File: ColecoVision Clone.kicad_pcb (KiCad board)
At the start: 2 copper layers, 149.4 x 99.1 mm, 143 parts, among them J1 Cartridge Slot, J2 Composite video, J3 PJ-102A, J4 RCJ-017, J5 Controller Port 1, J6 Controller Port 2, Q1 2n4401, Q2 Q_NJFET_DGS, Q3 2N3904, Q4 2N3904, Q5 2N3904, SW1 Power Toggle, SW2 Reset, U1 Z80CPU, U10 SN76489AN, U12 74LS138 (Mem. Mapped), U13 74LS138 (I/O), U14 74LS02, U15 Controller 1, U16 Controller 2, U17 74LS05, U18 74LS05, U19 74HC04, U2 Work RAM, U20 74LS74, U21 74HC04, U22 74LS74, U23 74HCT00, U24 TPS60403DBVR, U3 BIOS ROM 27C256, U4 74HCT04, U5 TMS9918A, U6 74LS574, U7 74LS574, U8 74LS574, U9 VRAM, X1 14.31818MHz

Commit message: powering chips
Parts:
- C4, R15: moved to B.Cu
- moved R1 191.3 mm to (24.6, 47.9)
- moved C4 99.2 mm to (52.5, 39.9), turned to 90 degrees
- moved R15 90.1 mm to (32.3, 67.6), turned to 90 degrees
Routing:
- net VCC: track 650.9 -> 742.4 mm, vias 30 -> 39
- net GND: track 745.0 -> 771.3 mm, vias 38 -> 40
- net !WAIT: track 125.4 -> 134.8 mm
- net /Video/VIDVCC: track 4.64 -> 11.0 mm
- net AD1: track 105.0 -> 98.9 mm
- net Net-(R15-Pad2): track 0.00 -> 4.93 mm
- net RW: track 71.8 -> 75.1 mm
- net D1: track 289.9 -> 288.8 mm
- net RAM_A1: track 23.7 -> 22.7 mm
- net RAM_A0: track 24.1 -> 23.4 mm
- net AD3: track 91.3 -> 92.0 mm
- net AD0: track 96.5 -> 95.9 mm

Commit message: HALT pullup
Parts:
- removed TP13: TestPoint, Measurement_Points:Measurement_Point_Round-SMD-Pad_Small
- R44: moved to B.Cu
- moved R44 307.0 mm to (-56.0, 82.7)
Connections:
- net !HALT renamed Net-(R44-Pad2)
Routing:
- net Net-(R44-Pad2): track 5.94 -> 44.9 mm, vias 1 -> 8
- net VCC: track 742.4 -> 749.3 mm, vias 39 -> 40
- net D3: track 270.1 -> 269.6 mm

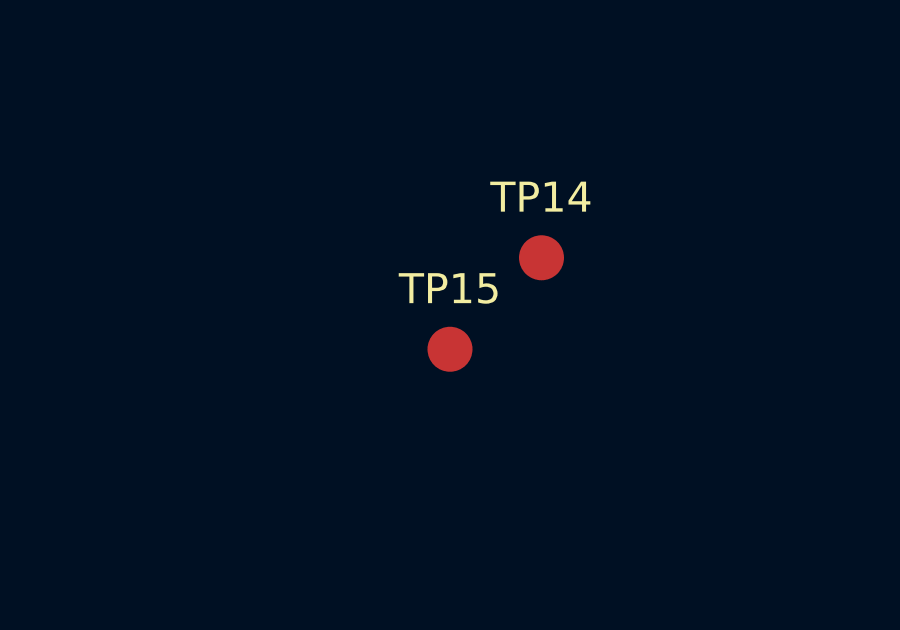
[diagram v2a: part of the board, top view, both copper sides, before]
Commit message: Goodbye A15 testpoint
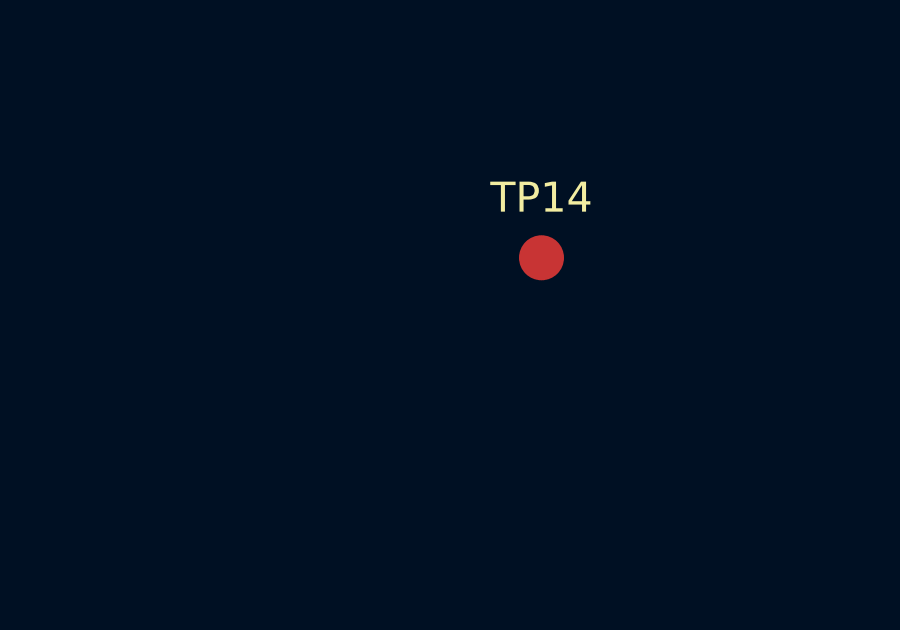
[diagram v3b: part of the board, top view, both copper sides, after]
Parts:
- removed TP15: TestPoint, Measurement_Points:Measurement_Point_Round-SMD-Pad_Small
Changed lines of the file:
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@@
     (tracks 4351)
     (zones 0)
-    (modules 142)
+    (modules 141)
     (nets 198)
   )
@@
   )
   (module Measurement_Points:Measurement_Point_Round-SMD-Pad_Small (layer F.Cu)
-    (at 223.978 114.307)
-    (descr "Mesurement Point, Round, SMD Pad, DM 1.5mm,")
-    (tags "Mesurement Point Round SMD Pad 1.5mm")
-    (attr virtual)
-    (fp_text reference TP15 (at 0 -2) (layer F.SilkS)
-      (effects (font (size 1 1) (thickness 0.15)))
-    )
-    (fp_text value TestPoint (at 0 2) (layer F.Fab)
-      (effects (font (size 1 1) (thickness 0.15)))
-    )
-    (fp_circle (center 0 0) (end 1 0) (layer F.CrtYd) (width 0.05))
-    (pad 1 smd circle (at 0 0) (size 1.5 1.5) (layers F.Cu F.Mask)
-      (net 107 A15))
-  )
-  (module Measurement_Points:Measurement_Point_Round-SMD-Pad_Small (layer F.Cu)

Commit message: Controller port passives
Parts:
- C37, C38, R42: moved to B.Cu
- moved C38 156.8 mm to (-0.83, 118.1), turned to 270 degrees
- moved C37 144.1 mm to (9.46, 105.9), turned to 180 degrees
- moved R42 132.0 mm to (25.5, 122.0)
- moved R43 128.7 mm to (24.3, 112.6), turned to 270 degrees
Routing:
- net /Controllers/CTRL_PIN_8: track 37.5 -> 86.4 mm, vias 0 -> 6
- net GND: track 771.3 -> 798.0 mm, vias 40 -> 41
- net /Controllers/CTRL_PIN_5: track 39.5 -> 63.1 mm, vias 0 -> 2
- net Net-(R41-Pad1): track 5.47 -> 10.8 mm
- net Net-(R40-Pad2): track 18.7 -> 23.2 mm
- net CTRL_EN_1: track 54.1 -> 51.7 mm
- net !INT: track 172.8 -> 171.1 mm
- net !NMI: track 113.8 -> 112.3 mm
- net D3: track 269.6 -> 269.0 mm

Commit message: Reset passives
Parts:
- C21, C32, R16, R17: moved to B.Cu
- moved R16 179.1 mm to (51.3, 124.8)
- moved R17 172.0 mm to (46.3, 124.8)
- moved C21 166.0 mm to (56.3, 124.8)
- moved C32 109.1 mm to (58.1, 118.9)
- moved C31 87.1 mm to (64.1, 125.3)
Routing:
- net Net-(C32-Pad2): track 11.4 -> 39.5 mm
- net Net-(C32-Pad1): track 105.5 -> 129.1 mm, vias 2 -> 4
- net Net-(C31-Pad2): track 7.46 -> 30.6 mm
- net GND: track 798.0 -> 817.5 mm, vias 41 -> 43
- net Net-(C21-Pad1): track 25.9 -> 41.0 mm
- net VCC: track 749.3 -> 752.2 mm, vias 40 -> 41
- net Net-(C31-Pad1): track 212.3 -> 214.9 mm

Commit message: Special U24 cap
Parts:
- C40, R23: moved to B.Cu
- moved R8 265.0 mm to (7.11, 30.5)
- moved C40 187.8 mm to (44.2, 110.5), turned to 270 degrees
- moved TP14 159.1 mm to (72.2, 74.4)
- moved R21 157.0 mm to (70.2, 78.4)
- moved R23 115.4 mm to (54.9, 85.6), turned to 90 degrees
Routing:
- net Net-(C30-Pad1): track 189.1 -> 87.2 mm, vias 10 -> 9
- net !RESET: track 114.5 -> 149.4 mm, vias 9 -> 11
- net VCC: track 752.2 -> 778.9 mm, vias 41 -> 42
- net !WAIT: track 134.8 -> 155.4 mm, vias 4 -> 6
- net Net-(R44-Pad2): track 44.9 -> 39.0 mm, vias 8 -> 7
- net GND: track 817.5 -> 813.3 mm, vias 43 -> 41
- net Net-(C3-Pad2): track 35.3 -> 37.5 mm, vias 0 -> 1
- net (no net): track 1.95 -> 0.00 mm, vias 1 -> 0
- net !WR: track 86.7 -> 85.7 mm

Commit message: Silence DRC
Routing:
- net Net-(C30-Pad1): track 87.2 -> 193.3 mm, vias 9 -> 10
- net GND: track 813.3 -> 798.9 mm, vias 41 -> 39
- net !WAIT: track 155.4 -> 142.7 mm, vias 6 -> 5
- net VCC: track 778.9 -> 776.6 mm
- net Net-(J6-Pad6): track 79.5 -> 78.4 mm
- net !INT: track 171.1 -> 172.1 mm

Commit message: Bits and bobs - ready for decouplers
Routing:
- net GND: track 798.9 -> 841.0 mm, vias 39 -> 47
- net !WAIT: track 142.7 -> 159.1 mm
- net D1: track 288.6 -> 287.0 mm
- net D0: track 265.2 -> 264.3 mm
- net CPU_CLK: track 153.2 -> 152.5 mm
- net D5: track 286.7 -> 287.2 mm
